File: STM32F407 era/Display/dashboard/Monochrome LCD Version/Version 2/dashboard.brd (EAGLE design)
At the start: 200 x 75.1 mm, 93 parts, among them IC2 74HC14D, IC3 74HC14D, U1 CAT4238TD-GT3

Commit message: created Gerbers
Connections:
- net BTN1S: now also U$1.P$24; no longer U$1.P$23
- net BTN2S: now also U$1.P$26; no longer U$1.P$24
- net BTN3S: now also U$1.P$30; no longer U$1.P$25
- net BTN4S: now also U$1.P$35; no longer U$1.P$28
- net BTN5S: now also U$1.P$28; no longer U$1.P$26
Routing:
- net BTN3S: track 27.3 -> 22.7 mm
- net BTN1S: track 24.4 -> 22.8 mm
- net BTN5S: track 27.3 -> 26.5 mm
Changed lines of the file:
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@@
 </signal>
 <signal name="BTN1S">
-<contactref element="U$1" pad="P$23"/>
 <contactref element="IC2" pad="2"/>
 <wire x1="203.9366" y1="64.4525" x2="205.4225" y2="64.4525" width="0.4064" layer="1"/>
 <via x="205.4225" y="64.4525" extent="1-16" drill="0.381"/>
-<wire x1="205.4225" y1="64.4525" x2="205.4225" y2="66.9925" width="0.4064" layer="16"/>
-<wire x1="205.4225" y1="66.9925" x2="193.9925" y2="78.4225" width="0.4064" layer="16"/>
-<wire x1="193.9925" y1="78.4225" x2="193.9925" y2="80.645" width="0.4064" layer="16"/>
-<wire x1="193.9925" y1="80.645" x2="195.38315" y2="82.03565" width="0.4064" layer="16"/>
-<wire x1="195.38315" y1="82.03565" x2="195.38315" y2="82.04835" width="0.4064" layer="16"/>
+<contactref element="U$1" pad="P$24"/>
+<wire x1="205.4225" y1="64.4525" x2="205.4225" y2="73.025" width="0.4064" layer="16"/>
+<wire x1="205.4225" y1="73.025" x2="200.9775" y2="77.47" width="0.4064" layer="16"/>
+<wire x1="200.9775" y1="77.47" x2="197.4215" y2="77.47" width="0.4064" layer="16"/>
+<wire x1="197.4215" y1="77.47" x2="195.38315" y2="79.50835" width="0.4064" layer="16"/>
 </signal>
 <signal name="BTN2S">
-<contactref element="U$1" pad="P$24"/>
 <contactref element="IC2" pad="4"/>
 <wire x1="203.9366" y1="61.9125" x2="205.4225" y2="61.9125" width="0.4064" layer="1"/>
 <via x="205.4225" y="61.9125" extent="1-16" drill="0.381"/>
 <wire x1="205.4225" y1="61.9125" x2="206.375" y2="62.865" width="0.4064" layer="16"/>
-<wire x1="206.375" y1="62.865" x2="206.375" y2="66.9925" width="0.4064" layer="16"/>
-<wire x1="206.375" y1="66.9925" x2="195.38315" y2="77.98435" width="0.4064" layer="16"/>
-<wire x1="195.38315" y1="77.98435" x2="195.38315" y2="79.50835" width="0.4064" layer="16"/>
+<contactref element="U$1" pad="P$26"/>
+<wire x1="206.375" y1="62.865" x2="206.375" y2="73.025" width="0.4064" layer="16"/>
+<wire x1="206.375" y1="73.025" x2="201.295" y2="78.105" width="0.4064" layer="16"/>
+<wire x1="201.295" y1="78.105" x2="199.3265" y2="78.105" width="0.4064" layer="16"/>
+<wire x1="199.3265" y1="78.105" x2="197.92315" y2="79.50835" width="0.4064" layer="16"/>
 </signal>
 <signal name="BTN3S">
-<contactref element="U$1" pad="P$25"/>
 <contactref element="IC2" pad="10"/>
 <wire x1="210.0834" y1="60.6425" x2="208.5975" y2="60.6425" width="0.4064" layer="1"/>
 <via x="208.5975" y="60.6425" extent="1-16" drill="0.381"/>
 <wire x1="208.5975" y1="60.6425" x2="207.645" y2="61.595" width="0.4064" layer="16"/>
-<wire x1="207.645" y1="61.595" x2="207.645" y2="67.6275" width="0.4064" layer="16"/>
-<wire x1="207.645" y1="67.6275" x2="199.0725" y2="76.2" width="0.4064" layer="16"/>
-<wire x1="199.0725" y1="76.2" x2="199.0725" y2="80.899" width="0.4064" layer="16"/>
-<wire x1="199.0725" y1="80.899" x2="197.92315" y2="82.04835" width="0.4064" layer="16"/>
+<contactref element="U$1" pad="P$30"/>
+<wire x1="207.645" y1="61.595" x2="207.645" y2="73.66" width="0.4064" layer="16"/>
+<wire x1="207.645" y1="73.66" x2="203.00315" y2="78.30185" width="0.4064" layer="16"/>
+<wire x1="203.00315" y1="78.30185" x2="203.00315" y2="79.50835" width="0.4064" layer="16"/>
 </signal>
 <signal name="BTN4S">
@@
 <wire x1="210.0834" y1="63.1825" x2="208.5975" y2="63.1825" width="0.4064" layer="1"/>
 <via x="208.5975" y="63.1825" extent="1-16" drill="0.381"/>
-<wire x1="208.5975" y1="63.1825" x2="208.5975" y2="67.6275" width="0.4064" layer="16"/>
-<wire x1="208.5975" y1="67.6275" x2="200.46315" y2="75.76185" width="0.4064" layer="16"/>
-<contactref element="U$1" pad="P$28"/>
-<wire x1="200.46315" y1="75.76185" x2="200.46315" y2="79.50835" width="0.4064" layer="16"/>
+<contactref element="U$1" pad="P$35"/>
+<wire x1="208.5975" y1="63.1825" x2="208.5975" y2="78.105" width="0.4064" layer="16"/>
+<wire x1="208.5975" y1="78.105" x2="209.2325" y2="78.74" width="0.4064" layer="16"/>
+<wire x1="209.2325" y1="78.74" x2="209.2325" y2="80.6577" width="0.4064" layer="16"/>
+<wire x1="209.2325" y1="80.6577" x2="210.62315" y2="82.04835" width="0.4064" layer="16"/>
 </signal>
 <signal name="BTN5S">
@@
 <via x="208.5975" y="58.1025" extent="1-16" drill="0.381"/>
 <wire x1="208.5975" y1="58.1025" x2="207.01" y2="59.69" width="0.4064" layer="16"/>
-<wire x1="207.01" y1="59.69" x2="207.01" y2="67.31" width="0.4064" layer="16"/>
-<wire x1="207.01" y1="67.31" x2="197.92315" y2="76.39685" width="0.4064" layer="16"/>
-<contactref element="U$1" pad="P$26"/>
-<wire x1="197.92315" y1="76.39685" x2="197.92315" y2="79.50835" width="0.4064" layer="16"/>
+<wire x1="207.01" y1="59.69" x2="207.01" y2="73.3425" width="0.4064" layer="16"/>
+<contactref element="U$1" pad="P$28"/>
+<wire x1="207.01" y1="73.3425" x2="200.84415" y2="79.50835" width="0.4064" layer="16"/>
+<wire x1="200.84415" y1="79.50835" x2="200.46315" y2="79.50835" width="0.4064" layer="16"/>
 </signal>
 <signal name="SW5">

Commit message: minor updates to power circuitry
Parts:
- removed D3: MBRS130LT3, diode:SMB
- added D2: (no value), diode:SMC
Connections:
- net GND: now also D2.A; no longer D3.A
- net N$6: now also D2.C; no longer D3.C
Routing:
- net N$6: track 22.0 -> 28.4 mm
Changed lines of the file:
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@@
 <element name="R3" library="microbuilder" package="_0603" value="1k" x="214.63" y="34.29" rot="MR270"/>
 <element name="L2" library="SparkFun-Passives" package="CDRH125" value="MSS1583-683MED" x="219.71" y="22.86" rot="MR90"/>
-<element name="D3" library="diode" package="SMB" value="MBRS130LT3" x="217.805" y="33.02" rot="MR270"/>
 <element name="C25" library="rcl" package="153CLV-1012" value="470u" x="227.33" y="34.925" rot="MR0"/>
 <element name="C26" library="rcl" package="153CLV-1012" value="220u" x="205.105" y="22.86" rot="MR180"/>
@@
 </element>
 <element name="PTC1" library="microbuilder" package="PTC1812" value="" x="237.8075" y="38.4175" rot="MR180"/>
+<element name="D2" library="diode" package="SMC" value="" x="231.14" y="23.1775" rot="MR270"/>
 </elements>
 <signals>
@@
 <contactref element="IC1" pad="6"/>
 <contactref element="IC1" pad="3"/>
-<contactref element="D3" pad="A"/>
 <contactref element="R3" pad="1"/>
 <contactref element="C25" pad="-"/>
@@
 <contactref element="C4" pad="1"/>
 <via x="86.0425" y="55.88" extent="1-16" drill="0.381"/>
+<contactref element="D2" pad="A"/>
 </signal>
 <signal name="N$1">
@@
 <contactref element="IC1" pad="2"/>
 <contactref element="L2" pad="1"/>
-<contactref element="D3" pad="C"/>
-<wire x1="211.5312" y1="36.6268" x2="216.3982" y2="36.6268" width="1.016" layer="16"/>
-<wire x1="216.3982" y1="36.6268" x2="217.805" y2="35.22" width="1.016" layer="16"/>
-<wire x1="217.805" y1="35.22" x2="217.805" y2="34.925" width="1.016" layer="16"/>
-<wire x1="217.805" y1="34.925" x2="224.61" y2="28.12" width="1.016" layer="16"/>
-<wire x1="224.61" y1="28.12" x2="224.61" y2="22.86" width="1.016" layer="16"/>
+<wire x1="216.1032" y1="36.6268" x2="224.61" y2="28.12" width="1.016" layer="16"/>
+<wire x1="224.61" y1="28.12" x2="224.61" y2="26.9875" width="1.016" layer="16"/>
+<contactref element="D2" pad="C"/>
+<wire x1="224.61" y1="26.9875" x2="224.61" y2="22.86" width="1.016" layer="16"/>
+<wire x1="216.1032" y1="36.6268" x2="211.5312" y2="36.6268" width="1.016" layer="16"/>
+<wire x1="231.14" y1="26.8775" x2="230.395" y2="26.9875" width="1.016" layer="16"/>
+<wire x1="230.395" y1="26.9875" x2="224.61" y2="26.9875" width="1.016" layer="16"/>
 </signal>
 <signal name="N$9">

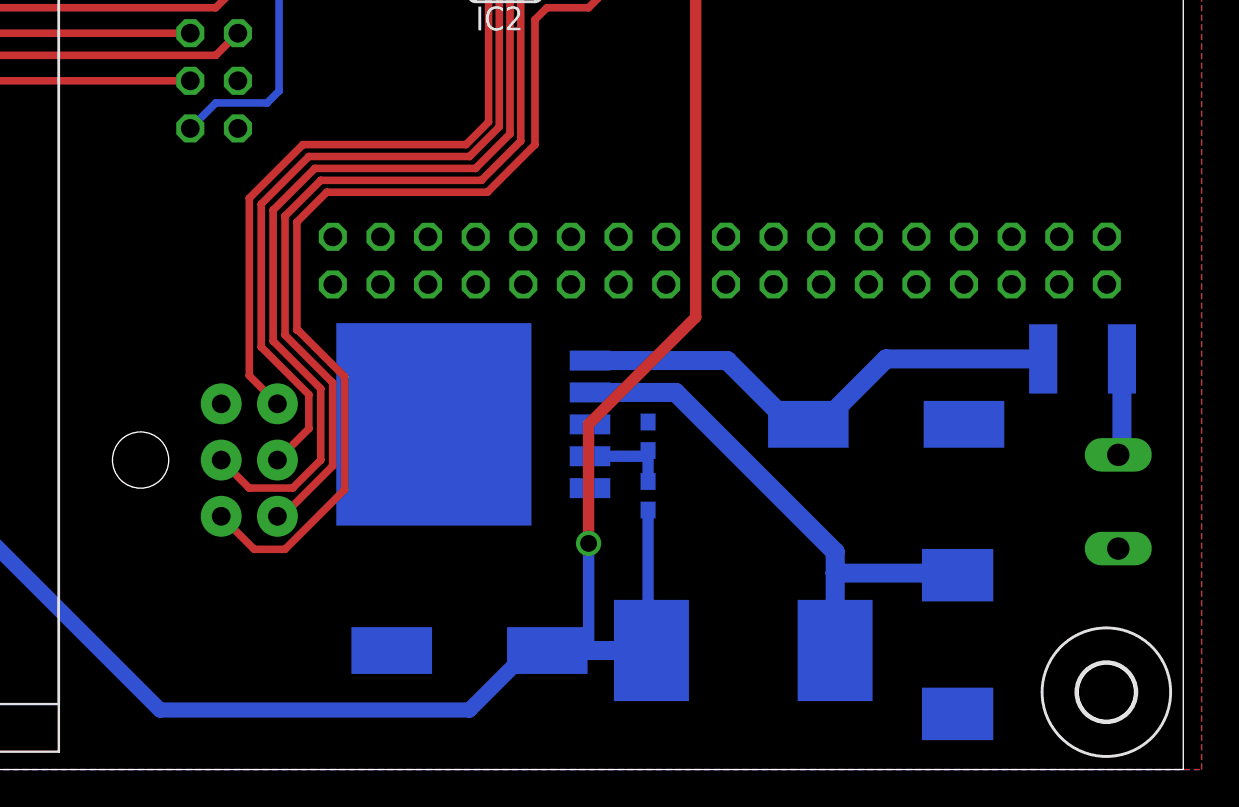
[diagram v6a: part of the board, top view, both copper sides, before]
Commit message: added testpoints to power rails and coms, and created new Gerbers for PCB order
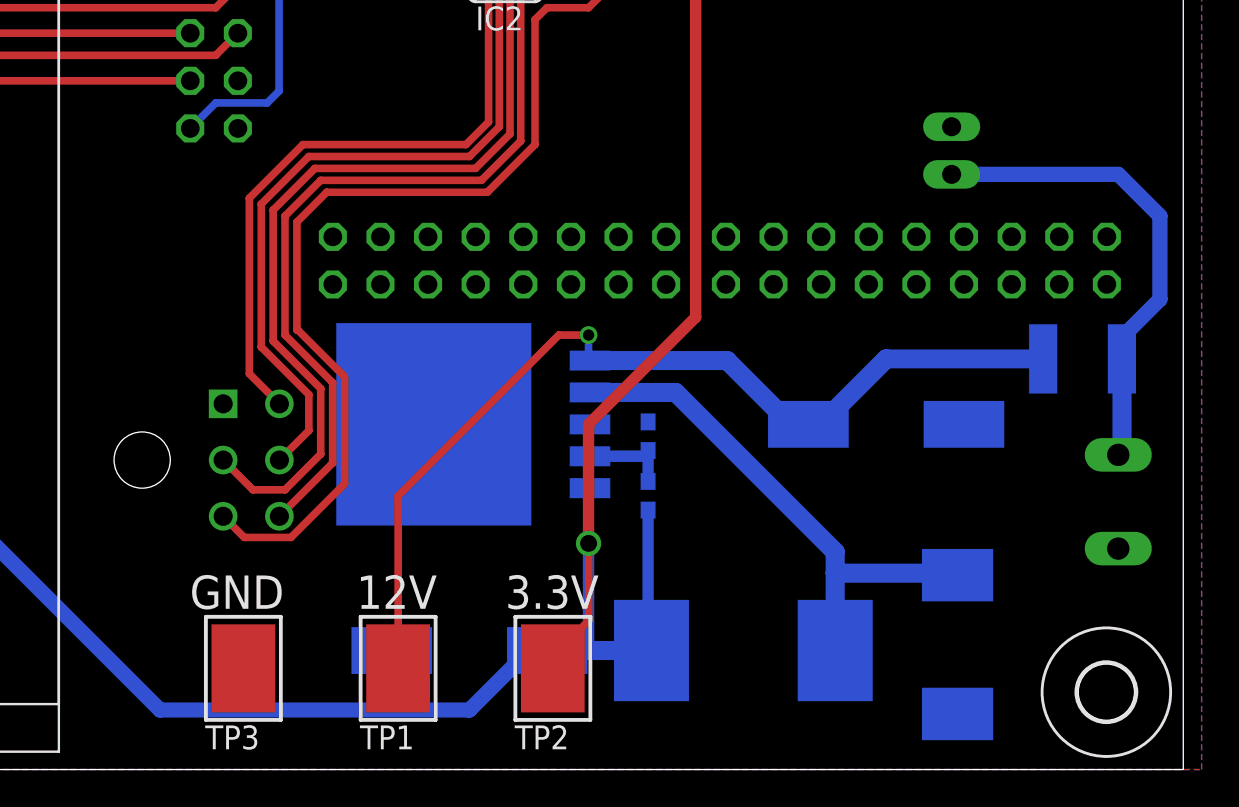
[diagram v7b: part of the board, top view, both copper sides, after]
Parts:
- added TP1, TP2, TP3: (no value), microbuilder:TESTPOINT_SMT
- added X2: 22-05-7028-02, con-molex:7395-02
- U$42: device unicorn:MICROFIT6SOCK -> unicorn:43045-0600
- moved U$42 5.71 mm to (187.6, 33.0)
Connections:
- removed net N$77: C25.+, IC1.1, PTC1.P$1
- new net VSUP: C25.+, IC1.1, PTC1.P$1, TP1.P$1
- net 12V: now also X2.1
- net 3.3V: now also TP2.P$1
- net BTN1: now also U$42.P$5; no longer U$42.PIN4
- net BTN2: now also U$42.P$4; no longer U$42.PIN2
- net BTN3: now also U$42.P$6; no longer U$42.PIN6
- net BTN4: now also U$42.P$2; no longer U$42.PIN3
- net BTN5: now also U$42.P$3; no longer U$42.PIN5
- net GND: now also TP3.P$1, U$42.P$1, X2.2; no longer U$42.PIN1
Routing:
- net VSUP: track 0.00 -> 51.5 mm, vias 0 -> 1
- net N$77: track 27.2 -> 0.00 mm
- net 12V: track 5.31 -> 25.8 mm
- net 3.3V: track 546.7 -> 554.1 mm
- net BTN5: track 53.8 -> 53.0 mm
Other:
- board text added: "+"
- board text added: "12V"
- board text added: "3.3V"
- board text added: "AUX Power"
- board text added: "GND"
